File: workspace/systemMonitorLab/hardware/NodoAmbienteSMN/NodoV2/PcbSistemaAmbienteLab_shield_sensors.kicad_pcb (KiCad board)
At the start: 2 copper layers, 30 x 47 mm, 6 parts, among them J5 Molex_Sensor_BMP280, J6 Molex_Sensor_DHT22, U2 Bmp280Module, U3 DHT22

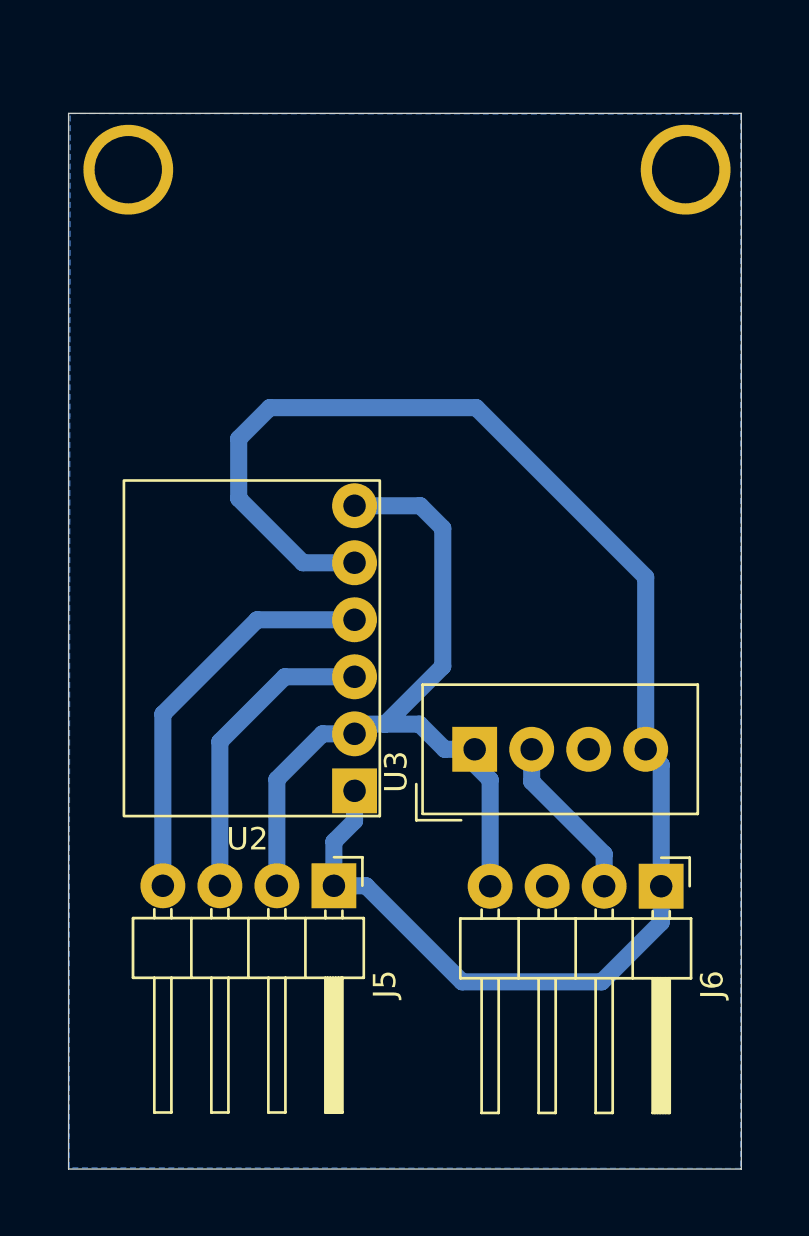
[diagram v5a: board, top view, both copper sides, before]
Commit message: Subo el resideño de los pcb's acorde al case 3d
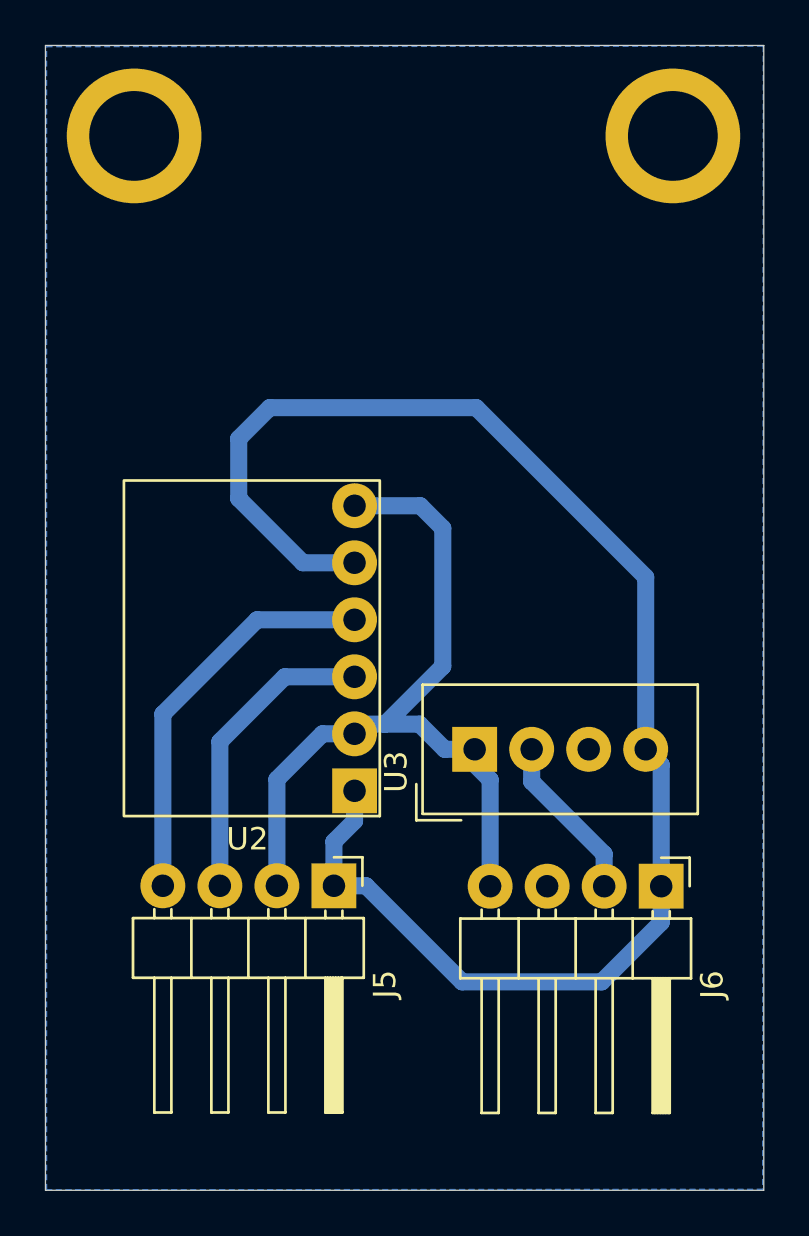
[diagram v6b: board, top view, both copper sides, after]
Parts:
- removed the ? at (155.7, 59.4)
- removed the ? at (180.6, 59.3)
- added ?: , , F.Cu at (180.0, 52.9)
- added ?: , , F.Cu at (156.0, 52.9)
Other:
- board size 30 x 47 mm -> 32 x 51 mm
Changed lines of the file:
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@@
 	(footprint ""
 		(layer "F.Cu")
-		(at 155.74 59.43)
+		(at 180 52.925)
 		(property "Reference" ""
 			(at 0 0 0)
@@
 		)
 		(pad "" thru_hole circle
-			(at 0 -5 180)
-			(size 4 4)
-			(drill 3)
-			(layers "*.Cu" "*.Mask")
-			(remove_unused_layers no)
-			(pinfunction "RV")
-			(pintype "bidirectional+no_connect")
-		)
-		(embedded_fonts no)
-	)
-	(footprint ""
-		(layer "F.Cu")
-		(at 180.57 59.28)
-		(property "Reference" ""
-			(at 0 0 0)
-			(layer "F.SilkS")
-			(effects
-				(font
-					(size 1.27 1.27)
-					(thickness 0.15)
-				)
-			)
-		)
-		(property "Value" ""
-			(at 0 0 0)
-			(layer "F.Fab")
-			(effects
-				(font
-					(size 1.27 1.27)
-					(thickness 0.15)
-				)
-			)
-		)
-		(property "Datasheet" ""
-			(at 0 0 0)
-			(layer "F.Fab")
-			(hide yes)
-			(effects
-				(font
-					(size 1.27 1.27)
-					(thickness 0.15)
-				)
-			)
-		)
-		(property "Description" ""
-			(at 0 0 0)
-			(layer "F.Fab")
-			(hide yes)
-			(effects
-				(font
-					(size 1.27 1.27)
-					(thickness 0.15)
-				)
-			)
-		)
-		(pad "" thru_hole circle
-			(at 0 -4.85 180)
-			(size 4 4)
-			(drill 3)
+			(at 0 0 180)
+			(size 6 6)
+			(drill 4)
 			(layers "*.Cu" "*.Mask")
 			(remove_unused_layers no)
@@
 		)
 		(property "Value" "Molex_Sensor_BMP280"
-			(at 4.385 9.89 90)
+			(at 3.37 10.65 90)
 			(layer "F.Fab")
 			(effects
@@
 		)
 	)
+	(footprint ""
+		(layer "F.Cu")
+		(at 156 52.925)
+		(property "Reference" ""
+			(at 0 0 0)
+			(layer "F.SilkS")
+			(effects
+				(font
+					(size 1.27 1.27)
+					(thickness 0.15)
+				)
+			)
+		)
+		(property "Value" ""
+			(at 0 0 0)
+			(layer "F.Fab")
+			(effects
+				(font
+					(size 1.27 1.27)
+					(thickness 0.15)
+				)
+			)
+		)
+		(property "Datasheet" ""
+			(at 0 0 0)
+			(layer "F.Fab")
+			(hide yes)
+			(effects
+				(font
+					(size 1.27 1.27)
+					(thickness 0.15)
+				)
+			)
+		)
+		(property "Description" ""
+			(at 0 0 0)
+			(layer "F.Fab")
+			(hide yes)
+			(effects
+				(font
+					(size 1.27 1.27)
+					(thickness 0.15)
+				)
+			)
+		)
+		(pad "" thru_hole circle
+			(at 0 0 180)
+			(size 6 6)
+			(drill 4)
+			(layers "*.Cu" "*.Mask")
+			(remove_unused_layers no)
+			(pinfunction "RV")
+			(pintype "bidirectional+no_connect")
+		)
+		(embedded_fonts no)
+	)
 	(footprint "Sensors_commercial:BMP280_Module"
 		(layer "F.Cu")
@@
 	)
 	(gr_rect
-		(start 153.08 51.92)
-		(end 183.05 98.95)
+		(start 152.05 48.895)
+		(end 184.05 99.895)
 		(stroke
 			(width 0.05)
@@
 		(layer "Dwgs.User")
 		(pts
-			(xy 153.08 98.95) (xy 183.05 98.95)
-		)
-		(height 5.02)
-		(orientation 0)
+			(xy 184.05 48.895) (xy 184.05 99.895)
+		)
+		(height 9.5)
+		(orientation 1)
 		(format
 			(prefix "")
@@
 			(keep_text_aligned yes)
 		)
-		(gr_text "29.9700 mm"
-			(at 168.065 102.82 0)
+		(gr_text "51.0000 mm"
+			(at 192.4 74.395 90)
+			(layer "Dwgs.User")
+			(effects
+				(font
+					(size 1 1)
+					(thickness 0.15)
+				)
+			)
+		)
+	)
+	(dimension
+		(type orthogonal)
+		(layer "Dwgs.User")
+		(pts
+			(xy 152.05 98.95) (xy 184.05 98.95)
+		)
+		(height 5.575)
+		(orientation 0)
+		(format
+			(prefix "")
+			(suffix "")
+			(units 3)
+			(units_format 1)
+			(precision 4)
+		)
+		(style
+			(thickness 0.1)
+			(arrow_length 1.27)
+			(text_position_mode 0)
+			(arrow_direction outward)
+			(extension_height 0.58642)
+			(extension_offset 0.5)
+			(keep_text_aligned yes)
+		)
+		(gr_text "32.0000 mm"
+			(at 168.05 103.375 0)
+			(layer "Dwgs.User")
+			(effects
+				(font
+					(size 1 1)
+					(thickness 0.15)
+				)
+			)
+		)
+	)
+	(dimension
+		(type orthogonal)
+		(layer "Dwgs.User")
+		(pts
+			(xy 156 52.925) (xy 180 52.925)
+		)
+		(height -10.125)
+		(orientation 0)
+		(format
+			(prefix "")
+			(suffix "")
+			(units 3)
+			(units_format 1)
+			(precision 4)
+		)
+		(style
+			(thickness 0.1)
+			(arrow_length 1.27)
+			(text_position_mode 0)
+			(arrow_direction outward)
+			(extension_height 0.58642)
+			(extension_offset 0.5)
+			(keep_text_aligned yes)
+		)
+		(gr_text "24.0000 mm"
+			(at 168 41.65 0)
 			(layer "Dwgs.User")
 			(effects
@@
 		(polygon
 			(pts
-				(xy 153.15 51.925) (xy 183.025 51.95) (xy 183.025 98.925) (xy 153.1 98.9)
-			)
-		)
+				(xy 152.1 48.95) (xy 184.025 48.925) (xy 184 99.85) (xy 152.1 99.875)
+			)
+		)

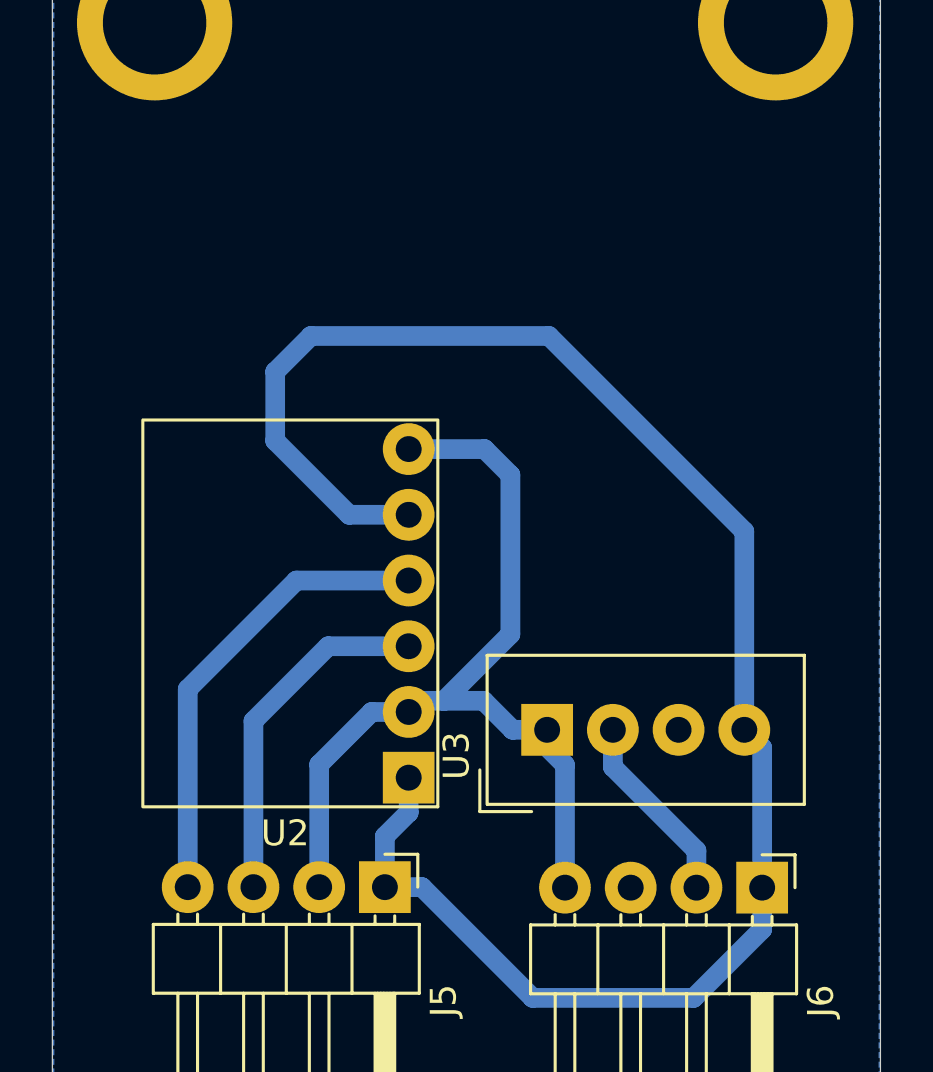
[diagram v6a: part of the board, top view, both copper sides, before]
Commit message: Tareas Realizadas: 	- Se corrije la disposicion de los conectores, para que el cable 	  quede derecho en su construccion se tiene que invertir el 	  orden de los pines en las placas led_status y sensors. 	- Se Cambio el ancho de las pistas que atraviesan a los 	  resistores SMD de 30 a 25 mils. 	- Se esta transmitiendo al sevirdor nginx por el puerto 80. Tareas proximas: 	- Se debe Contruir las placas y realizar pruebas. 	- Modificar el firmware para que los led envien los estados por 	  PWM para el LED dual. y On - OFF para el Led simple. 	- Se debe agregar un filtro para que los datos que tengan una 	  varianza mayor a un valor x no se transmitan. 	- Se debe agregar un retardo para que no se transmitan los datos 	  de inicio del barometro, ya que siempre marcan un valor 	  alredeor de 700 hPa.
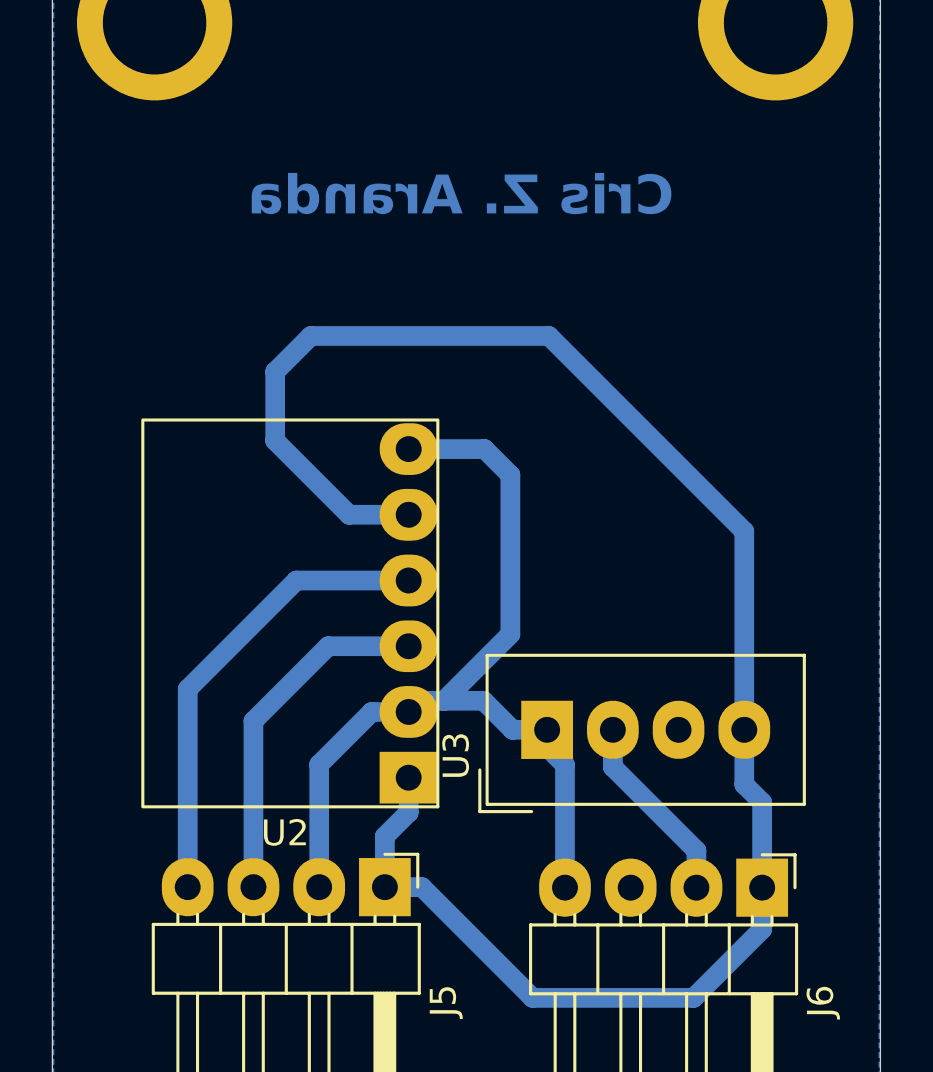
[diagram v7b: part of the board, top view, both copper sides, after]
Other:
- board text added: "Cris Z. Aranda"
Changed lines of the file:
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@@
 		(pad "1" thru_hole rect
 			(at 0 0 270)
-			(size 2 2)
+			(size 2.25 2)
 			(drill 1)
 			(layers "*.Cu" "*.Mask")
@@
 		(pad "2" thru_hole oval
 			(at 0 2.54 270)
-			(size 2 2)
+			(size 2.25 2)
 			(drill 1)
 			(layers "*.Cu" "*.Mask")
@@
 		(pad "3" thru_hole oval
 			(at 0 5.08 270)
-			(size 2 2)
+			(size 2.25 2)
 			(drill 1)
 			(layers "*.Cu" "*.Mask")
@@
 		(pad "4" thru_hole oval
 			(at 0 7.62 270)
-			(size 2 2)
+			(size 2.25 2)
 			(drill 1)
 			(layers "*.Cu" "*.Mask")
@@
 		(pad "1" thru_hole rect
 			(at 0 0 90)
-			(size 2 2)
+			(size 2.25 2)
 			(drill 1)
 			(layers "*.Cu" "*.Mask")
@@
 			(pintype "power_in")
 		)
-		(pad "2" thru_hole circle
+		(pad "2" thru_hole oval
 			(at 0 2.54 90)
-			(size 2 2)
+			(size 2.25 2)
 			(drill 1)
 			(layers "*.Cu" "*.Mask")
@@
 			(pintype "bidirectional")
 		)
-		(pad "3" thru_hole circle
+		(pad "3" thru_hole oval
 			(at 0 5.08 90)
-			(size 2 2)
+			(size 2.25 2)
 			(drill 1)
 			(layers "*.Cu" "*.Mask")
@@
 			(pintype "no_connect")
 		)
-		(pad "4" thru_hole circle
+		(pad "4" thru_hole oval
 			(at 0 7.62 90)
-			(size 2 2)
+			(size 2.25 2)
 			(drill 1)
 			(layers "*.Cu" "*.Mask")
@@
 		(pad "1" thru_hole rect
 			(at 0 0 270)
-			(size 2 2)
+			(size 2.25 2)
 			(drill 1)
 			(layers "*.Cu" "*.Mask")
@@
 		(pad "2" thru_hole oval
 			(at 0 2.54 270)
-			(size 2 2)
+			(size 2.25 2)
 			(drill 1)
 			(layers "*.Cu" "*.Mask")
@@
 		(pad "3" thru_hole oval
 			(at 0 5.08 270)
-			(size 2 2)
+			(size 2.25 2)
 			(drill 1)
 			(layers "*.Cu" "*.Mask")
@@
 		(pad "4" thru_hole oval
 			(at 0 7.62 270)
-			(size 2 2)
+			(size 2.25 2)
 			(drill 1)
 			(layers "*.Cu" "*.Mask")
@@
 		(pad "1" thru_hole rect
 			(at 0 0 180)
-			(size 2 2)
+			(size 2.25 2)
 			(drill 1)
 			(layers "*.Cu" "*.Mask")
@@
 			(pintype "power_in")
 		)
-		(pad "2" thru_hole circle
+		(pad "2" thru_hole oval
 			(at 0 2.54 180)
-			(size 2 2)
+			(size 2.25 2)
 			(drill 1)
 			(layers "*.Cu" "*.Mask")
@@
 			(pintype "power_in")
 		)
-		(pad "3" thru_hole circle
+		(pad "3" thru_hole oval
 			(at 0 5.08 180)
-			(size 2 2)
+			(size 2.25 2)
 			(drill 1)
 			(layers "*.Cu" "*.Mask")
@@
 			(pintype "bidirectional")
 		)
-		(pad "4" thru_hole circle
+		(pad "4" thru_hole oval
 			(at 0 7.62 180)
-			(size 2 2)
+			(size 2.25 2)
 			(drill 1)
 			(layers "*.Cu" "*.Mask")
@@
 			(pintype "bidirectional")
 		)
-		(pad "5" thru_hole circle
+		(pad "5" thru_hole oval
 			(at 0 10.16 180)
-			(size 2 2)
+			(size 2.25 2)
 			(drill 1)
 			(layers "*.Cu" "*.Mask")
@@
 			(pintype "input")
 		)
-		(pad "6" thru_hole circle
+		(pad "6" thru_hole oval
 			(at 0 12.7 180)
-			(size 2 2)
+			(size 2.25 2)
 			(drill 1)
 			(layers "*.Cu" "*.Mask")
@@
 		(fill no)
 		(layer "Edge.Cuts")
+	)
+	(gr_text "Cris Z. Aranda"
+		(at 176.075 60.475 0)
+		(layer "B.Cu")
+		(effects
+			(font
+				(size 1.5 1.5)
+				(thickness 0.375)
+				(bold yes)
+			)
+			(justify left bottom mirror)
+		)
 	)
 	(dimension
@@
 	)
 	(segment
-		(start 178.79 80.25)
-		(end 179.48 80.94)
-		(width 0.762)
-		(layer "B.Cu")
-		(net 1)
-	)
-	(segment
-		(start 179.48 80.94)
+		(start 179.48 83.055)
 		(end 179.48 86.35)
 		(width 0.762)
@@
 	)
 	(segment
+		(start 178.79 82.365)
+		(end 179.48 83.055)
+		(width 0.762)
+		(layer "B.Cu")
+		(net 1)
+	)
+	(segment
 		(start 171.24 65.03)
 		(end 178.79 72.58)
@@
 		(start 179.48 87.962)
 		(end 176.832 90.61)
+		(width 0.762)
+		(layer "B.Cu")
+		(net 1)
+	)
+	(segment
+		(start 178.79 80.25)
+		(end 178.79 82.365)
 		(width 0.762)
 		(layer "B.Cu")
@@
 		(hatch edge 0.5)
 		(connect_pads
-			(clearance 1)
-		)
-		(min_thickness 0.25)
+			(clearance 1.2)
+		)
+		(min_thickness 1)
 		(filled_areas_thickness no)
 		(fill yes
-			(thermal_gap 0.5)
-			(thermal_bridge_width 0.5)
+			(thermal_gap 0.1)
+			(thermal_bridge_width 3)
 		)
 		(polygon
